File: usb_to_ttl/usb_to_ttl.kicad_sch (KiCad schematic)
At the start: 15 parts, among them J1 Debug, P1 USB_C_Plug_USB2.0, P2 USB_C_Plug_USB2.0, U1 CP2102N-Axx-xQFN28, U2 TLV1117-33

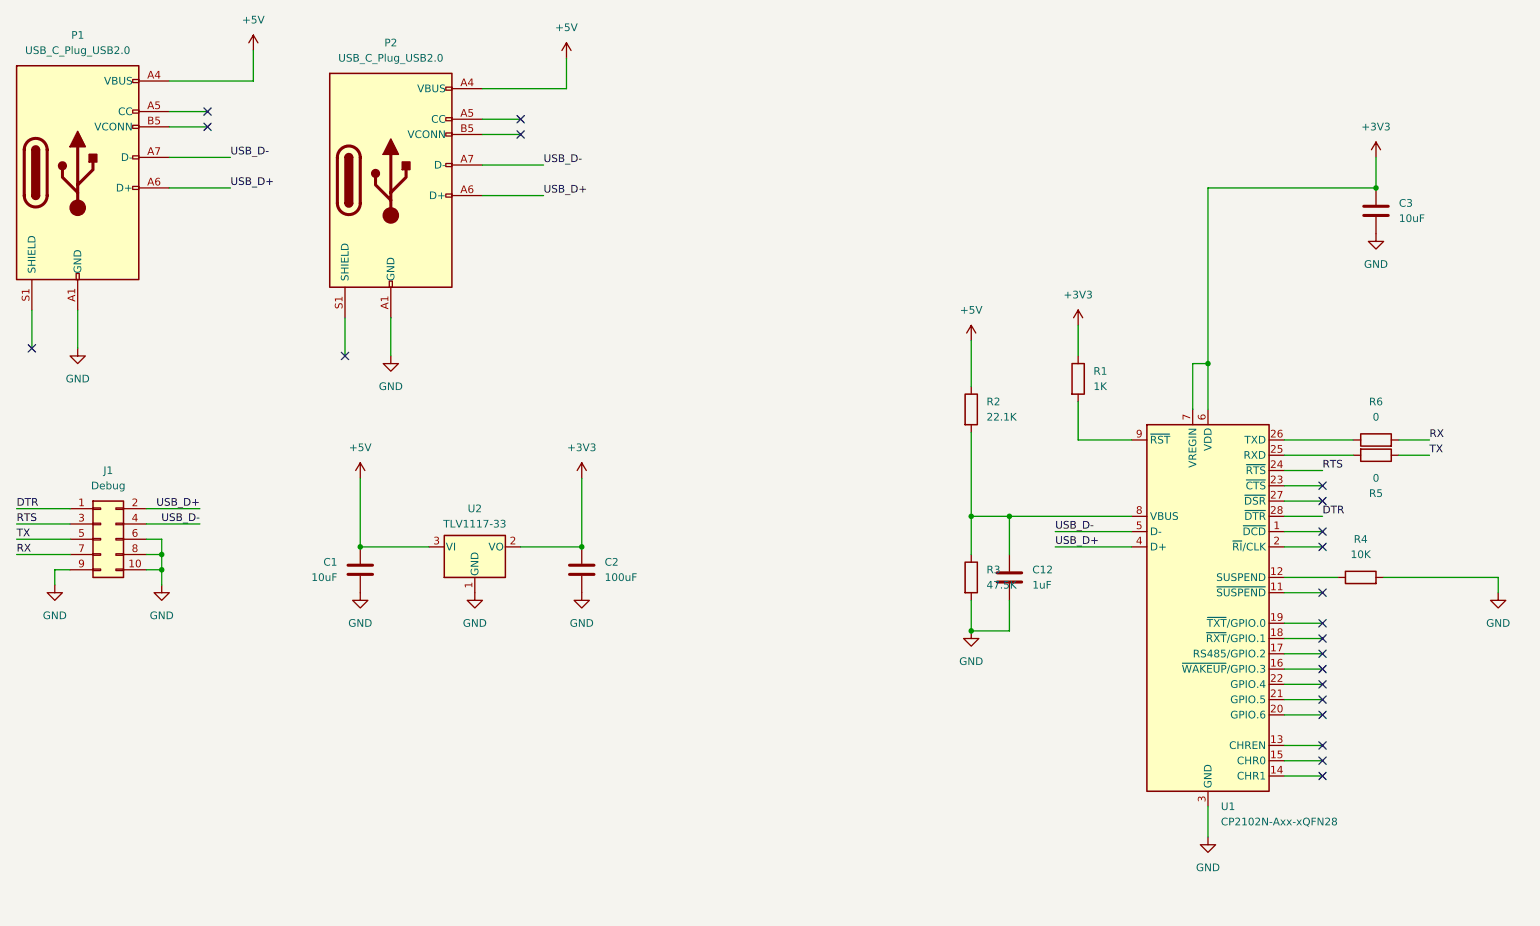
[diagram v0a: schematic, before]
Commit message: Updated adapter/debugger schematic and PCB files
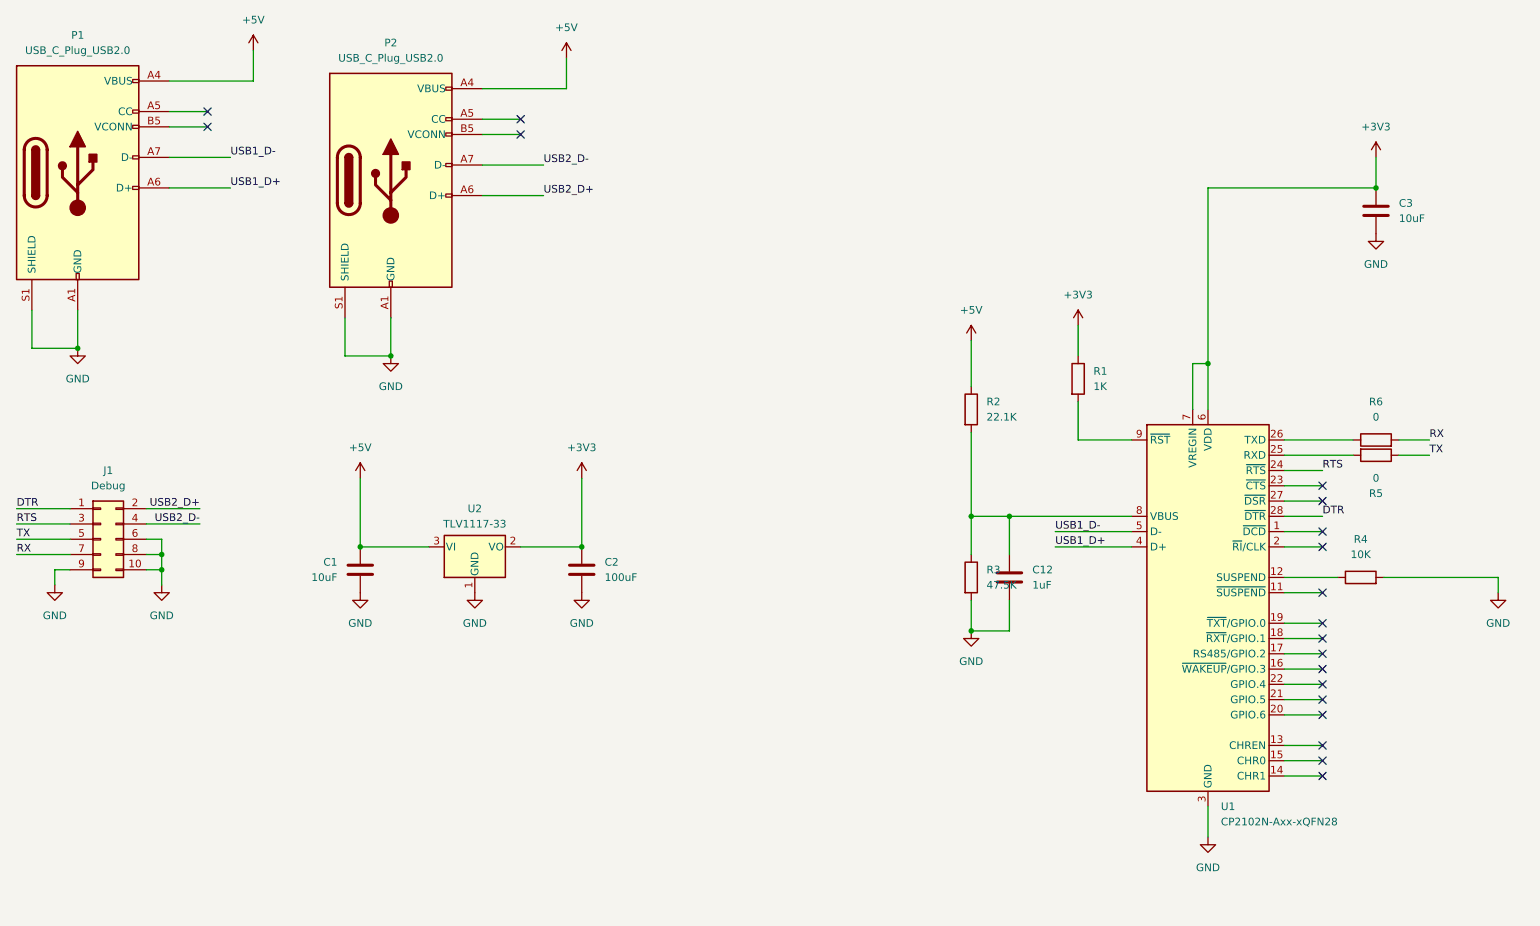
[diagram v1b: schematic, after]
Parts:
- P1, P2: footprint Connector_USB:USB_C_Plug_Molex_105444 -> Connector_USB:USB_C_Receptacle_G-Switch_GT-USB-7010ASV
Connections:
- net GND: now also P1.S1 (SHIELD), P2.S1 (SHIELD)
- net USB_D+ renamed USB1_D+
- net USB1_D+: no longer J1.2 (Pin_2), P2.A6 (D+)
- net USB_D- renamed USB1_D-
- net USB1_D-: no longer J1.4 (Pin_4), P2.A7 (D-)
- new net USB2_D+: J1.2 (Pin_2), P2.A6 (D+)
- new net USB2_D-: J1.4 (Pin_4), P2.A7 (D-)
- no-connect marks 21 -> 19
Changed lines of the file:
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@@
 	)
 	(junction
+		(at 29.21 67.31)
+		(diameter 0)
+		(color 0 0 0 0)
+	)
+	(junction
+		(at 81.28 68.58)
+		(diameter 0)
+		(color 0 0 0 0)
+	)
+	(junction
 		(at 43.18 101.6)
 		(diameter 0)
@@
 	)
 	(no_connect
-		(at 21.59 67.31)
-	)
-	(no_connect
 		(at 236.22 135.89)
 	)
@@
 	)
 	(no_connect
-		(at 73.66 68.58)
-	)
-	(no_connect
 		(at 236.22 90.17)
 	)
@@
 	(wire
 		(pts
+			(xy 73.66 68.58) (xy 81.28 68.58)
+		)
+		(stroke
+			(width 0)
+			(type default)
+		)
+	)
+	(wire
+		(pts
 			(xy 113.03 88.9) (xy 113.03 100.33)
 		)
@@
 	(wire
 		(pts
+			(xy 21.59 67.31) (xy 29.21 67.31)
+		)
+		(stroke
+			(width 0)
+			(type default)
+		)
+	)
+	(wire
+		(pts
 			(xy 229.87 100.33) (xy 236.22 100.33)
 		)
@@
 		)
 	)
-	(label "USB_D-"
+	(label "USB1_D-"
 		(at 191.77 97.79 0)
 		(effects
@@
 		)
 	)
-	(label "USB_D-"
+	(label "USB2_D-"
 		(at 106.68 36.83 0)
 		(effects
@@
 		)
 	)
-	(label "USB_D+"
+	(label "USB1_D+"
 		(at 54.61 40.64 0)
 		(effects
@@
 		)
 	)
-	(label "USB_D-"
+	(label "USB1_D-"
 		(at 54.61 35.56 0)
 		(effects
@@
 		)
 	)
-	(label "USB_D+"
+	(label "USB2_D+"
 		(at 49.53 93.98 180)
 		(effects
@@
 		)
 	)
-	(label "USB_D+"
+	(label "USB1_D+"
 		(at 191.77 100.33 0)
 		(effects
@@
 		)
 	)
-	(label "USB_D+"
+	(label "USB2_D+"
 		(at 106.68 41.91 0)
 		(effects
@@
 		)
 	)
-	(label "USB_D-"
+	(label "USB2_D-"
 		(at 49.53 96.52 180)
 		(effects
@@
 			)
 		)
-		(property "Footprint" "Connector_USB:USB_C_Plug_Molex_105444"
+		(property "Footprint" "Connector_USB:USB_C_Receptacle_G-Switch_GT-USB-7010ASV"
 			(at 33.02 38.1 0)
 			(effects
@@
 			)
 		)
-		(property "Footprint" "Connector_USB:USB_C_Plug_Molex_105444"
+		(property "Footprint" "Connector_USB:USB_C_Receptacle_G-Switch_GT-USB-7010ASV"
 			(at 85.09 39.37 0)
 			(effects

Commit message: USB to TTL Adapter design complete
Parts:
- C2: footprint Capacitor_SMD:C_0603_1608Metric -> Capacitor_SMD:C_0805_2012Metric
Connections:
- net RX: now also J1.5 (Pin_5); no longer J1.7 (Pin_7)
- net TX: now also J1.7 (Pin_7); no longer J1.5 (Pin_5)
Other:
- company: (none) -> jLab
- title: (none) -> USB to TTL Adapter
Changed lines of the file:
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@@
 	(generator_version "9.0")
 	(paper "A4")
+	(title_block
+		(title "USB to TTL Adapter")
+		(date "2025-09-27")
+		(rev "V1")
+		(company "jLab")
+	)
 	(junction
 		(at 245.11 40.64)
@@
 		)
 	)
-	(label "TX"
+	(label "RX"
 		(at 19.05 99.06 0)
 		(effects
@@
 		)
 	)
-	(label "RX"
+	(label "TX"
 		(at 19.05 101.6 0)
 		(effects
@@
 			)
 		)
-		(property "Footprint" "Capacitor_SMD:C_0603_1608Metric"
+		(property "Footprint" "Capacitor_SMD:C_0805_2012Metric"
 			(at 113.9952 107.95 0)
 			(effects

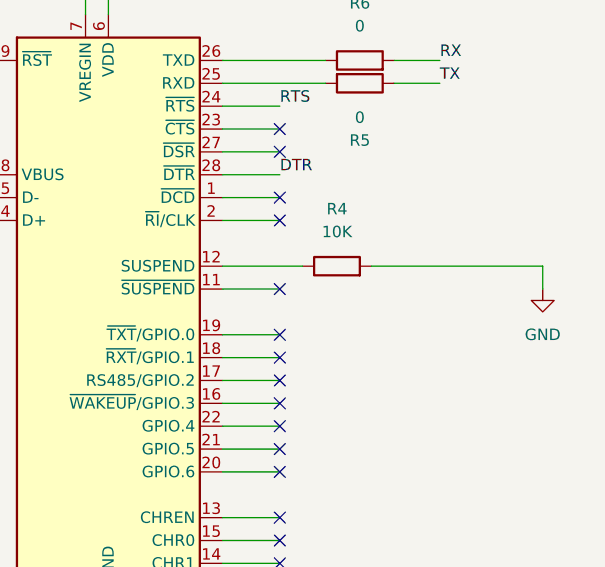
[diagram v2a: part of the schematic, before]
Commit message: Fixed connection to SUSPEND pins
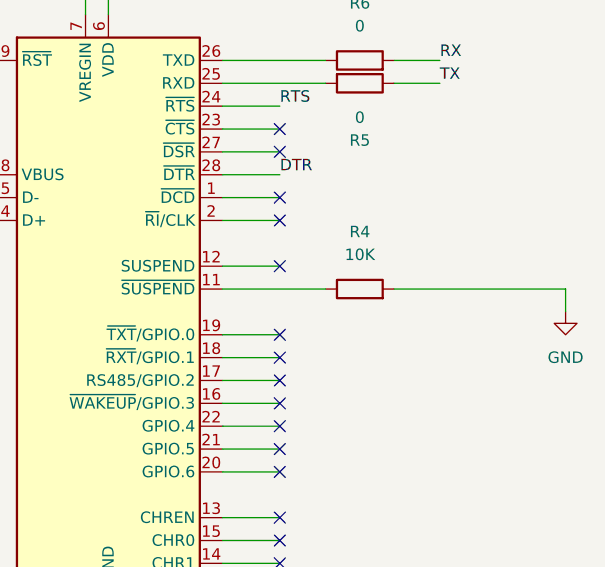
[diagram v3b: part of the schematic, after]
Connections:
- net at R4.1: now also U1.11 (~{SUSPEND}); no longer U1.12 (SUSPEND)
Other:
- moved on the sheet: R4
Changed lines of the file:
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@@
+	)
+	(no_connect
+		(at 236.22 105.41)
 	)
 	(no_connect
@@
 	)
 	(no_connect
-		(at 236.22 107.95)
-	)
-	(no_connect
 		(at 102.87 31.75)
 	)
@@
 	(wire
 		(pts
-			(xy 229.87 107.95) (xy 236.22 107.95)
+			(xy 229.87 107.95) (xy 241.3 107.95)
 		)
 		(stroke
@@
 	(wire
 		(pts
-			(xy 265.43 107.95) (xy 265.43 105.41)
+			(xy 267.97 110.49) (xy 267.97 107.95)
 		)
 		(stroke
@@
 	(wire
 		(pts
+			(xy 229.87 105.41) (xy 236.22 105.41)
+		)
+		(stroke
+			(width 0)
+			(type default)
+		)
+	)
+	(wire
+		(pts
 			(xy 229.87 133.35) (xy 236.22 133.35)
 		)
@@
 	(wire
 		(pts
-			(xy 265.43 105.41) (xy 246.38 105.41)
+			(xy 267.97 107.95) (xy 248.92 107.95)
 		)
 		(stroke
@@
 		(pts
 			(xy 217.17 40.64) (xy 217.17 69.85)
-		)
-		(stroke
-			(width 0)
-			(type default)
-		)
-	)
-	(wire
-		(pts
-			(xy 229.87 105.41) (xy 238.76 105.41)
 		)
 		(stroke
@@
 	(symbol
 		(lib_id "Device:R")
-		(at 242.57 105.41 90)
+		(at 245.11 107.95 90)
 		(unit 1)
 		(exclude_from_sim no)
@@
 		(fields_autoplaced yes)
 		(property "Reference" "R4"
-			(at 242.57 99.06 90)
+			(at 245.11 101.6 90)
 			(effects
 				(font
@@
 		)
 		(property "Value" "10K"
-			(at 242.57 101.6 90)
+			(at 245.11 104.14 90)
 			(effects
 				(font
@@
 		)
 		(property "Footprint" "Resistor_SMD:R_0603_1608Metric"
-			(at 242.57 107.188 90)
+			(at 245.11 109.728 90)
 			(effects
 				(font
@@
 		)
 		(property "Datasheet" "~"
-			(at 242.57 105.41 0)
+			(at 245.11 107.95 0)
 			(effects
 				(font
@@
 		)
 		(property "Description" "Resistor"
-			(at 242.57 105.41 0)
+			(at 245.11 107.95 0)
 			(effects
 				(font
@@
 	(symbol
 		(lib_id "power:GND")
-		(at 265.43 107.95 0)
+		(at 267.97 110.49 0)
 		(unit 1)
 		(exclude_from_sim no)
@@
 		(fields_autoplaced yes)
 		(property "Reference" "#PWR013"
-			(at 265.43 114.3 0)
+			(at 267.97 116.84 0)
 			(effects
 				(font
@@
 		)
 		(property "Value" "GND"
-			(at 265.43 113.03 0)
+			(at 267.97 115.57 0)
 			(effects
 				(font
@@
 		)
 		(property "Footprint" ""
-			(at 265.43 107.95 0)
+			(at 267.97 110.49 0)
 			(effects
 				(font
@@
 		)
 		(property "Datasheet" ""
-			(at 265.43 107.95 0)
+			(at 267.97 110.49 0)
 			(effects
 				(font
@@
 		)
 		(property "Description" "Power symbol creates a global label with name \"GND\" , ground"
-			(at 265.43 107.95 0)
-			(effects
-				(font
+			(at 267.97 110.49 0)
+			(effects
+				(font

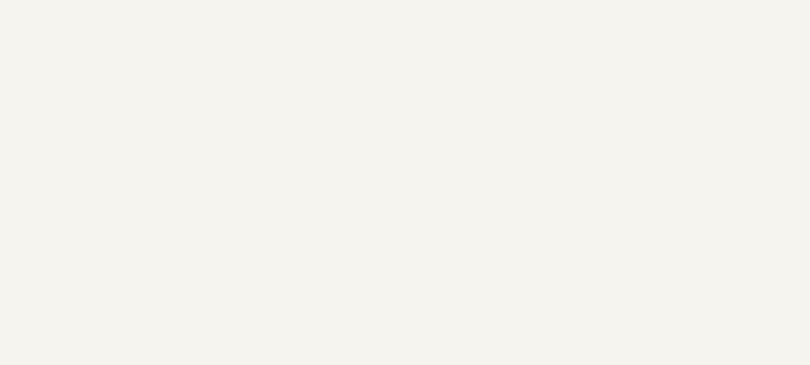
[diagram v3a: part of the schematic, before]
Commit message: Added mounting holes
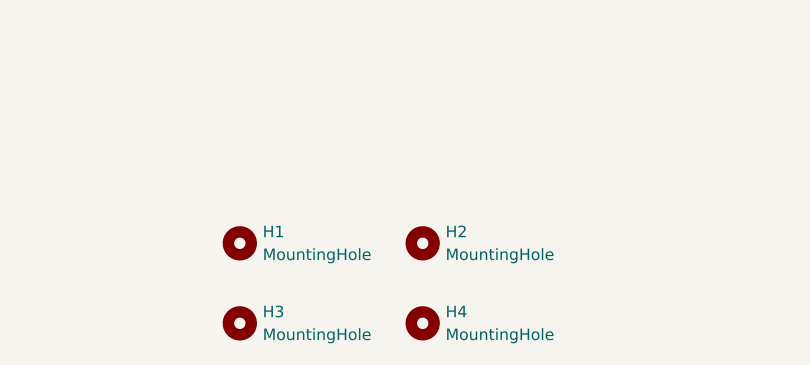
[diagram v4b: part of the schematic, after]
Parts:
- added H1, H2, H3, H4: MountingHole, MountingHole:MountingHole_3.2mm_M3_ISO7380, symbol Mechanical:MountingHole
